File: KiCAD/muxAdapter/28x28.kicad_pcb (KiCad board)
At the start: 4 copper layers, 30 x 30 mm, 55 parts, among them P1 CONN_01X01, P10 CONN_01X01, P11 CONN_01X01, P12 CONN_01X01, P13 CONN_01X01, P14 CONN_01X01, P15 CONN_01X01, P16 CONN_01X01, P17 CONN_01X01, P18 CONN_01X01, P19 CONN_01X01, P2 CONN_01X01, P20 CONN_01X01, P21 CONN_01X01, P22 CONN_01X01, P23 CONN_01X01, P24 CONN_01X01, P25 CONN_01X01, P26 CONN_01X01, P27 CONN_01X01, P28 CONN_01X01, P29 CONN_01X01, P3 CONN_01X01, P30 CONN_01X01, P31 CONN_01X01, P32 CONN_01X01, P33 CONN_01X01, P34 CONN_01X01, P35 CONN_01X01, P36 CONN_01X01, P37 CONN_01X01, P38 CONN_01X01, P39 CONN_01X02, P4 CONN_01X01, P40 CONN_01X02, P41 CONN_01X02, P42 CONN_01X02, P43 CONN_01X02, P44 CONN_01X02, P45 CONN_01X02, P46 CONN_01X02, P5 CONN_01X01, P6 CONN_01X01, P7 CONN_01X01, P8 CONN_01X01, P9 CONN_01X01, U1 MAX14662, U2 MAX14662, U3 PCF8574

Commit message: 28x28 mux adapter done28x28 mux adapter done
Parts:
- added G***: value, myparts:logo_small, F.Cu at (0.60, -10.2)
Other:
- board text added: "v0.21"

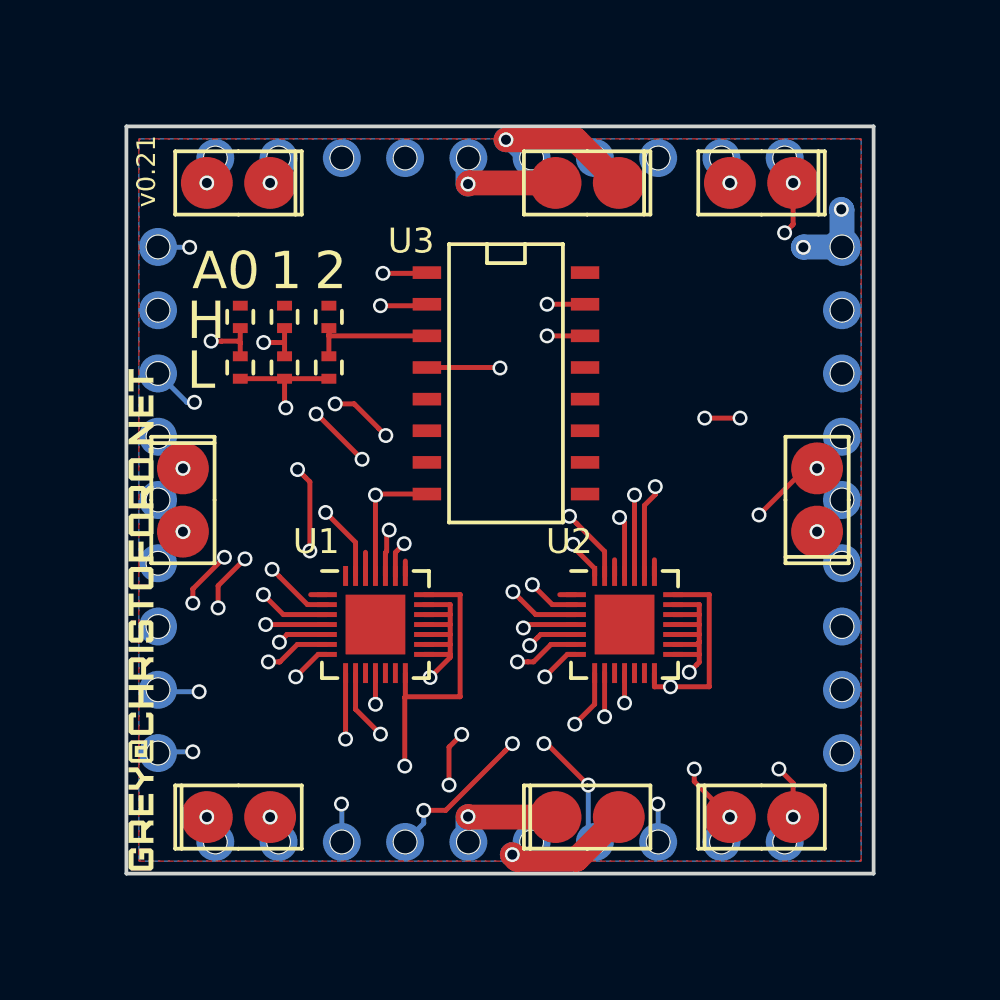
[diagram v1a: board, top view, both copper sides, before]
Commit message: order placed for 28x28 mux boards without blind vias
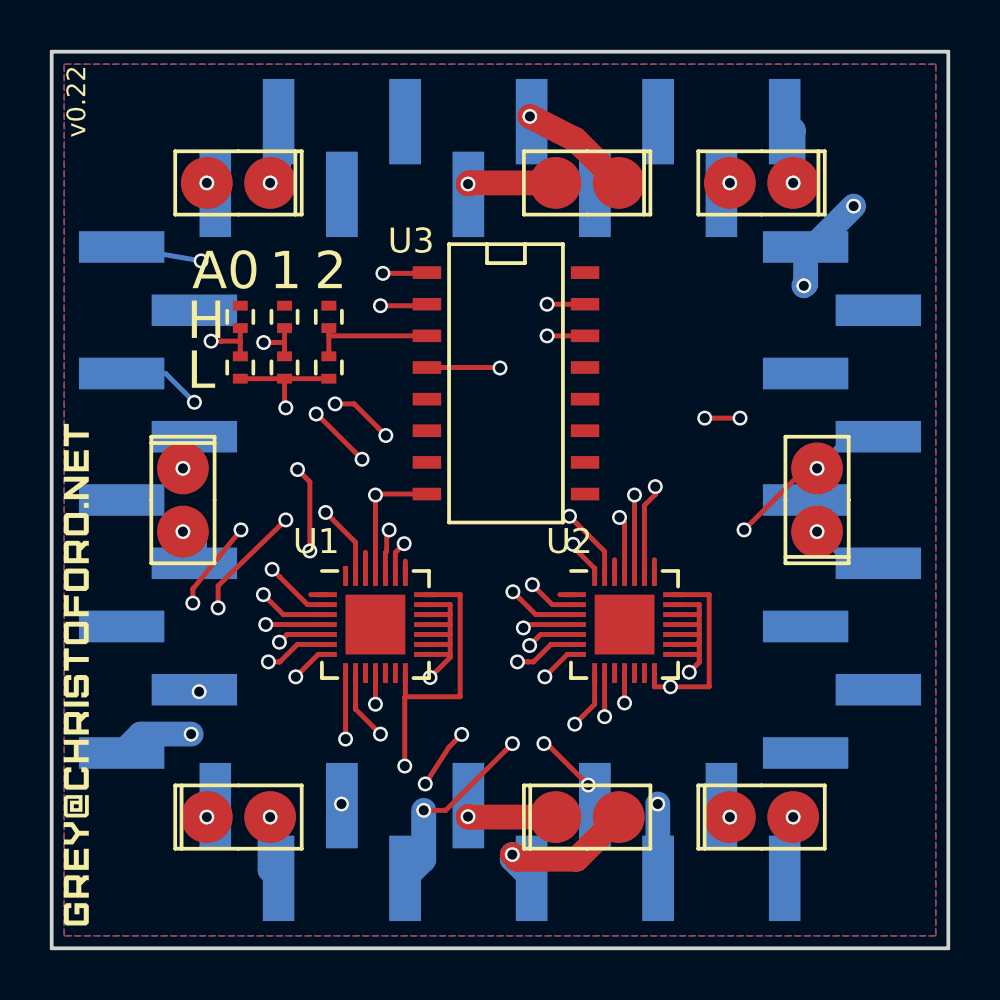
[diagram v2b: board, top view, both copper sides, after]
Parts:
- removed P1, P10, P11, P12, P13, P14, P15, P16, P17, P18, P19, P2, P20, P21, P22, P23, P24, P25, P26, P27, P28, P29, P3, P30, P31, P32, P33, P34, P35, P36, P37, P38, P4, P5, P6, P7, P8, P9: CONN_01X01, myparts:0508-0-00-15-00-00-03-0
- added P47: CONN_01X09, myparts:TSM-109-01-T-SV, B.Cu at (1.27, -25.2)
- added P48: CONN_01X10, myparts:TSM-110-01-T-SV, B.Cu at (3.57, -28.7)
- added P49: CONN_01X10, myparts:TSM-110-01-T-SV-INV, B.Cu at (3.57, -1.27)
- added P50: CONN_01X09, myparts:TSM-109-01-T-SV, B.Cu at (28.7, -25.2)
- moved G*** 3.41 mm to (-2.00, -8.00)
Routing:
- net V-: track 19.0 -> 16.6 mm, vias 4 -> 3
- net 2_V: track 37.6 -> 35.6 mm, vias 3 -> 2
- net 4_V: track 28.6 -> 30.6 mm, vias 4 -> 2
- net 5_V: track 14.6 -> 16.2 mm, vias 4 -> 2
- net I-: track 23.8 -> 25.3 mm, vias 3 -> 2
- net 3_V: track 19.9 -> 21.4 mm, vias 5 -> 4
- net SCK: track 38.1 -> 39.5 mm, vias 6 -> 5
- net 1_V: track 17.9 -> 19.4 mm, vias 3 -> 2
- net 0_V: track 39.9 -> 41.4 mm, vias 3 -> 2
- net V+: track 23.8 -> 25.2 mm, vias 4 -> 3
- net MOSI: track 33.3 -> 34.8 mm, vias 6 -> 5
- net SCL: track 27.4 -> 28.8 mm, vias 5 -> 4
- net R_I: track 27.4 -> 28.7 mm, vias 4 -> 3
- net R_V: track 16.9 -> 18.2 mm, vias 3 -> 2
- net 4_I: track 37.0 -> 35.9 mm, vias 5 -> 4
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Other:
- board size 30 x 30 mm -> 36 x 36 mm
- board text added: "v0.22"
- board text removed: "v0.21"

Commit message: fix some issues with the mux adapter board order
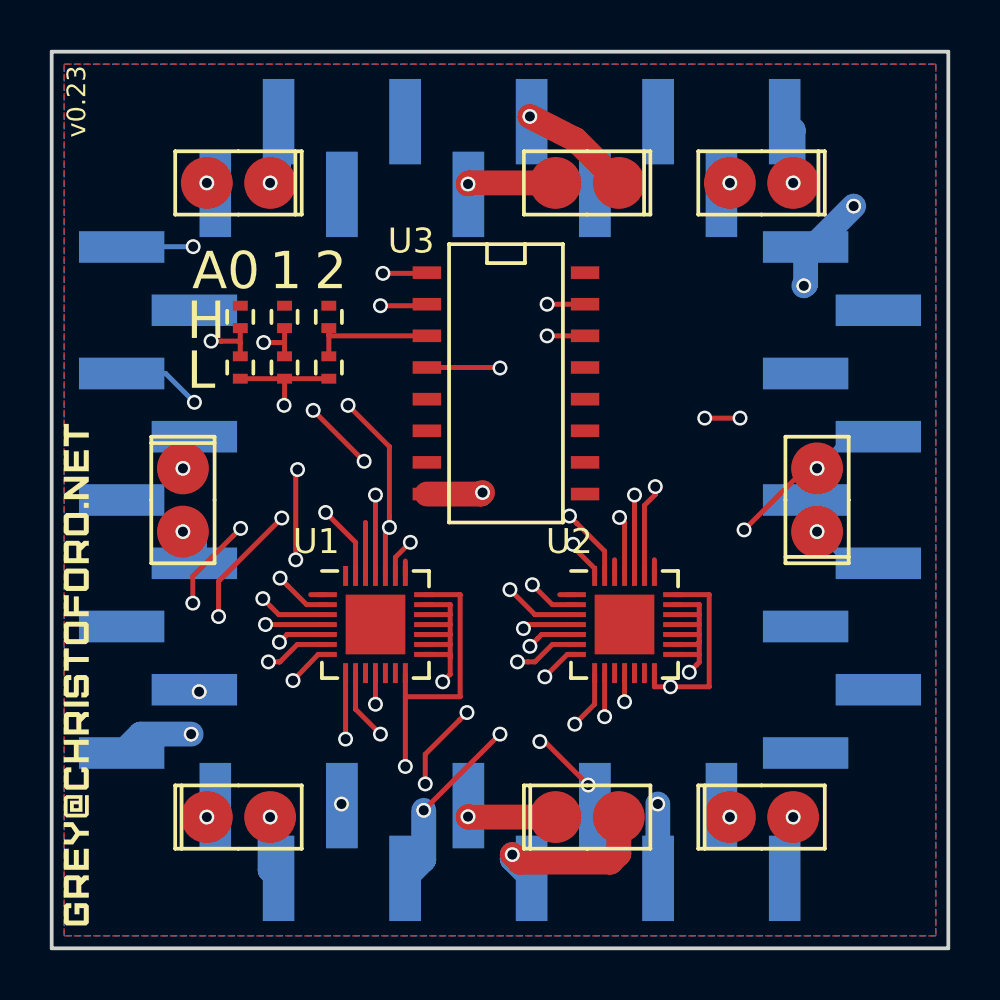
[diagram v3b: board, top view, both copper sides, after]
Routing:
- net SCK: track 39.5 -> 32.1 mm, vias 5 -> 4
- net L_V: track 20.9 -> 19.4 mm
- net +5V: track 8.35 -> 9.55 mm
- net 3_V: track 21.4 -> 22.5 mm
- net R_I: track 28.7 -> 27.8 mm
- net 4_I: track 35.9 -> 36.5 mm
- net GND: vias 5 -> 6
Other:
- net class Default: clearance 0.15 -> 0.16
- rule trace_clearance: 0.15 -> 0.16
- board text added: "v0.23"
- board text removed: "v0.22"

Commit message: fix up some hardware bugs
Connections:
- U1 pad 23: Net-(U1-Pad23) -> SM_CS
- U2 pad 28: Net-(U1-Pad23) -> (no net)
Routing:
- net SM_CS: track 14.9 -> 26.8 mm
- net Net-(U1-Pad23): track 9.83 -> 0.00 mm, vias 2 -> 0
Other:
- board text added: "v0.24"
- board text removed: "v0.23"

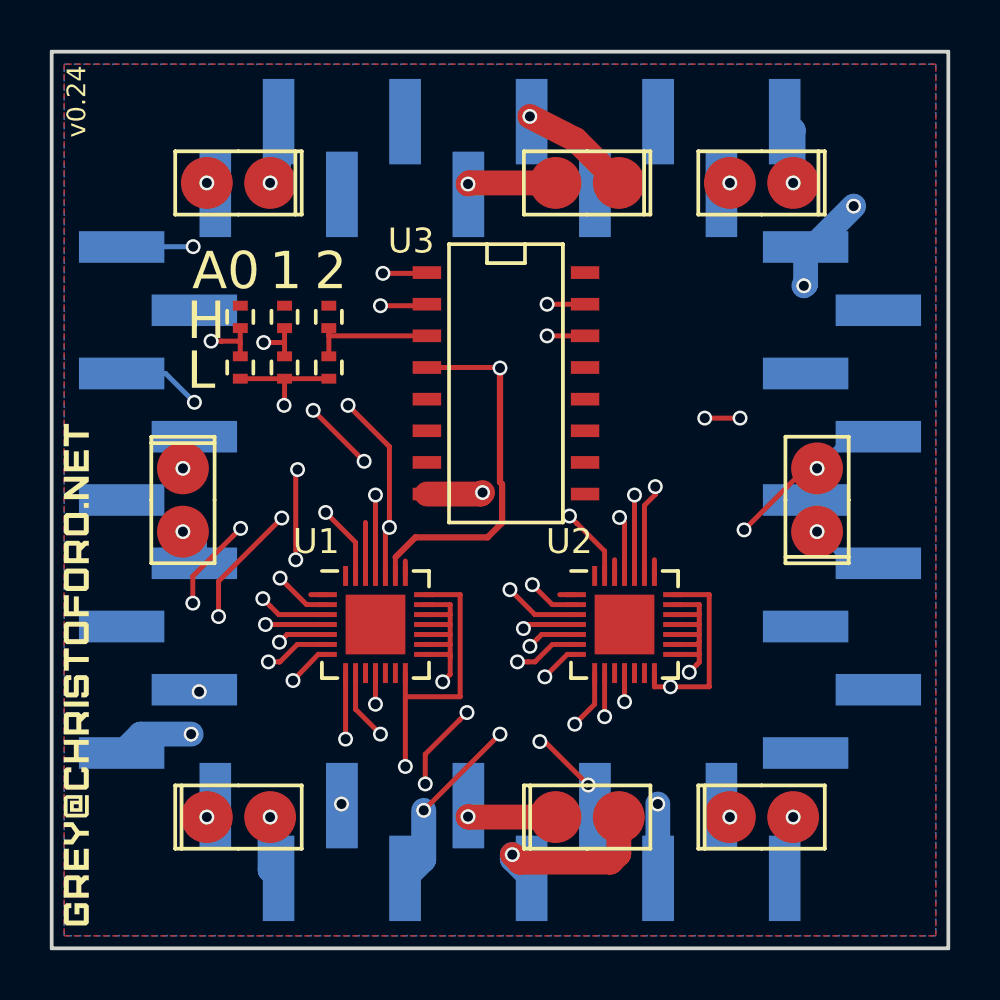
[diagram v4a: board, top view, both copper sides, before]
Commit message: fix 28x28 adapter chip width
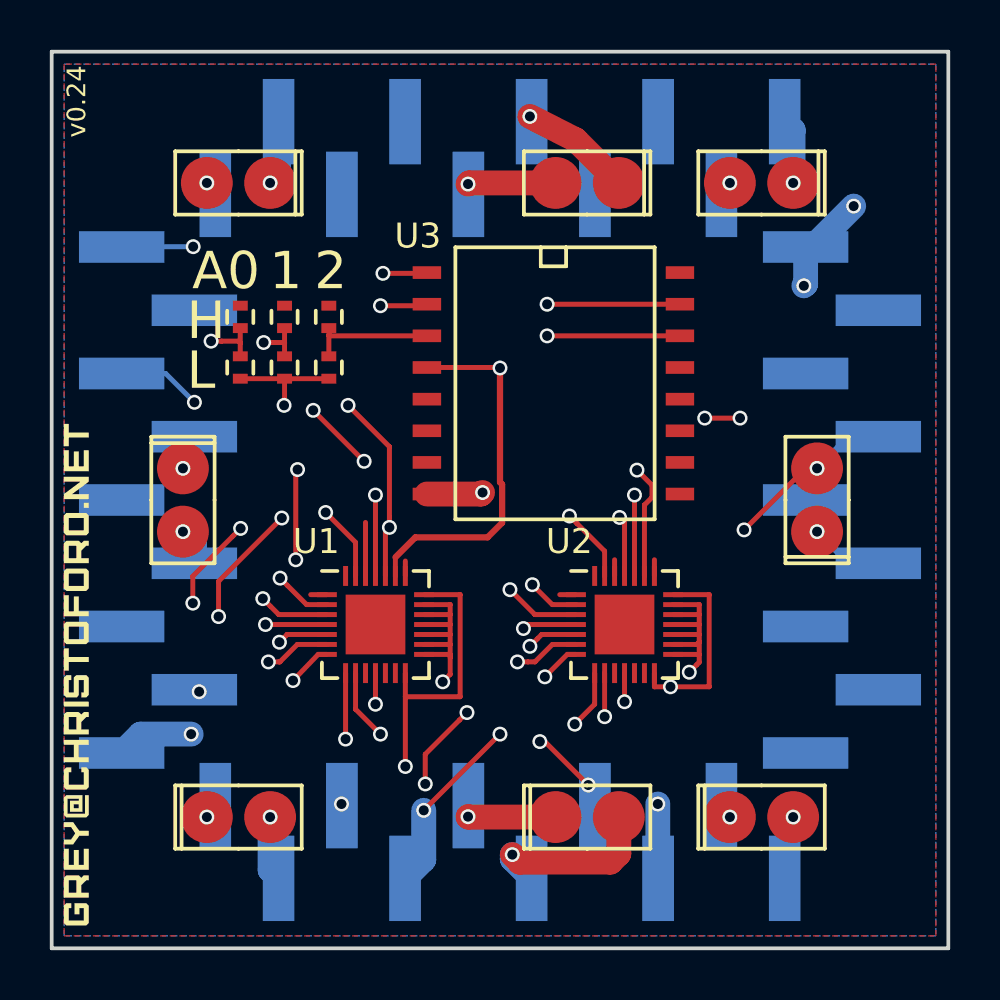
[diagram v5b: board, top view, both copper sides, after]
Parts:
- U3: footprint SMD_Packages:SO-16-N -> SMD_Packages:SO-16-W
- moved U3 1.90 mm to (17.1, -19.7)
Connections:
- P47 pad 2: (no net) -> Net-(P47-Pad2)
- P47 pad 5: (no net) -> Net-(P47-Pad5)
- P47 pad 7: (no net) -> Net-(P47-Pad7)
- P48 pad 3: (no net) -> Net-(P48-Pad3)
- P48 pad 4: (no net) -> Net-(P48-Pad4)
- P48 pad 7: (no net) -> Net-(P48-Pad7)
- P48 pad 8: (no net) -> Net-(P48-Pad8)
- P50 pad 2: (no net) -> +3V3
- P50 pad 3: (no net) -> Net-(P50-Pad3)
- P50 pad 5: (no net) -> Net-(P50-Pad5)
- P50 pad 7: (no net) -> Net-(P50-Pad7)
- P50 pad 8: (no net) -> Net-(P50-Pad8)
- U1 pad 10: (no net) -> Net-(U1-Pad10)
- U1 pad 12: (no net) -> Net-(U1-Pad12)
- U1 pad 13: (no net) -> Net-(U1-Pad13)
- U1 pad 28: (no net) -> Net-(U1-Pad28)
- U2 pad 10: (no net) -> Net-(U2-Pad10)
- U2 pad 12: (no net) -> Net-(U2-Pad12)
- U2 pad 13: (no net) -> Net-(U2-Pad13)
- U2 pad 28: (no net) -> Net-(U2-Pad28)
- U3 pad 10: (no net) -> Net-(U3-Pad10)
- U3 pad 11: (no net) -> Net-(U3-Pad11)
- U3 pad 12: (no net) -> Net-(U3-Pad12)
- U3 pad 13: (no net) -> Net-(U3-Pad13)
- U3 pad 5: (no net) -> Net-(U3-Pad5)
- U3 pad 6: (no net) -> Net-(U3-Pad6)
- U3 pad 7: (no net) -> Net-(U3-Pad7)
- U3 pad 9: (no net) -> Net-(U3-Pad9)
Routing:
- net SCL: track 28.5 -> 32.3 mm
- net SDA: track 26.7 -> 30.5 mm

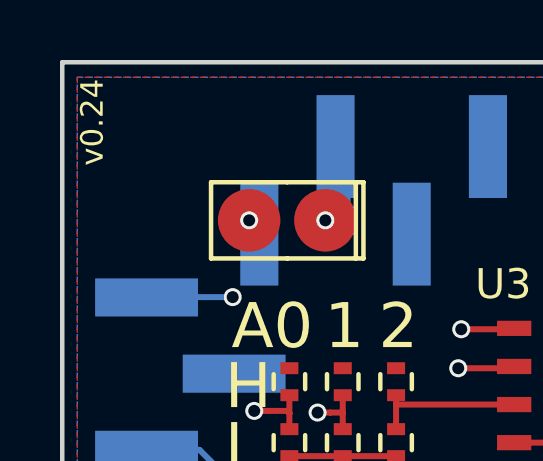
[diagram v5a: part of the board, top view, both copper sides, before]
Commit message: update board silkscreen version
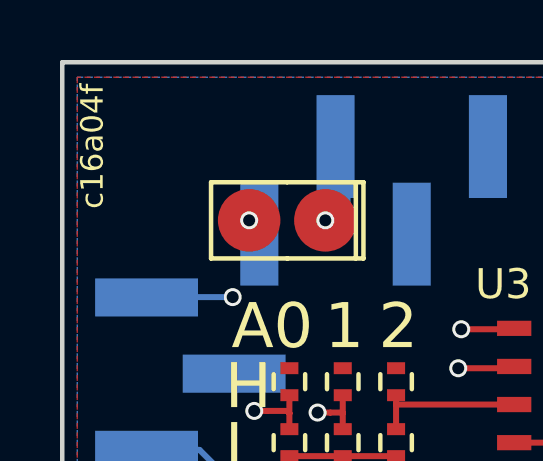
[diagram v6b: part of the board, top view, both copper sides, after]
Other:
- board text added: "c16a04f"
- board text removed: "v0.24"
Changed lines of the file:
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@@
   )
   (setup
-    (last_trace_width 0.2)
+    (last_trace_width 0.25)
     (user_trace_width 0.2)
     (user_trace_width 1)
@@
     )
   )
-  (gr_text v0.24 (at -2 -31 90) (layer F.SilkS)
+  (gr_text c16a04f (at -2 -30.2 90) (layer F.SilkS)
     (effects (font (size 0.75 0.75) (thickness 0.1875)))
   )
